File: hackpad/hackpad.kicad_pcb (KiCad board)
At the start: 2 copper layers, 18 parts, among them SW1 SW_Push_45deg, SW2 SW_Push_45deg, SW3 SW_Push_45deg, SW4 SW_Push_45deg, SW5 SW_Push_45deg, SW6 SW_Push_45deg, SW7 SW_Push_45deg, SW8 SW_Push_45deg, SW9 SW_Push_45deg

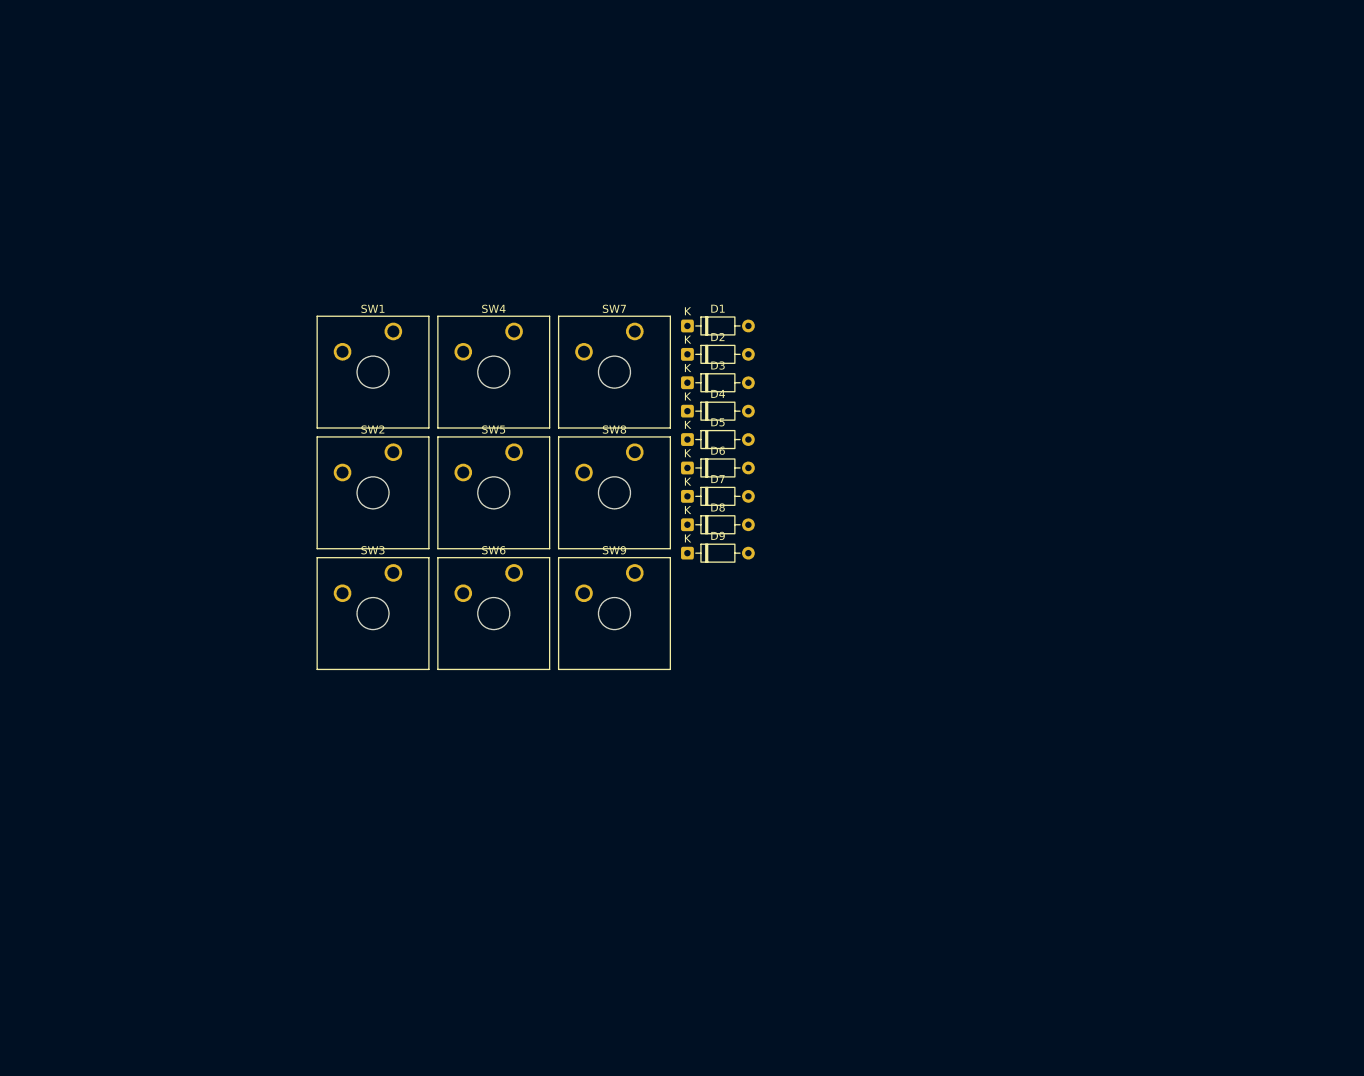
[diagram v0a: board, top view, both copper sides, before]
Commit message: Schematic Complete
Schematic complete currently routing
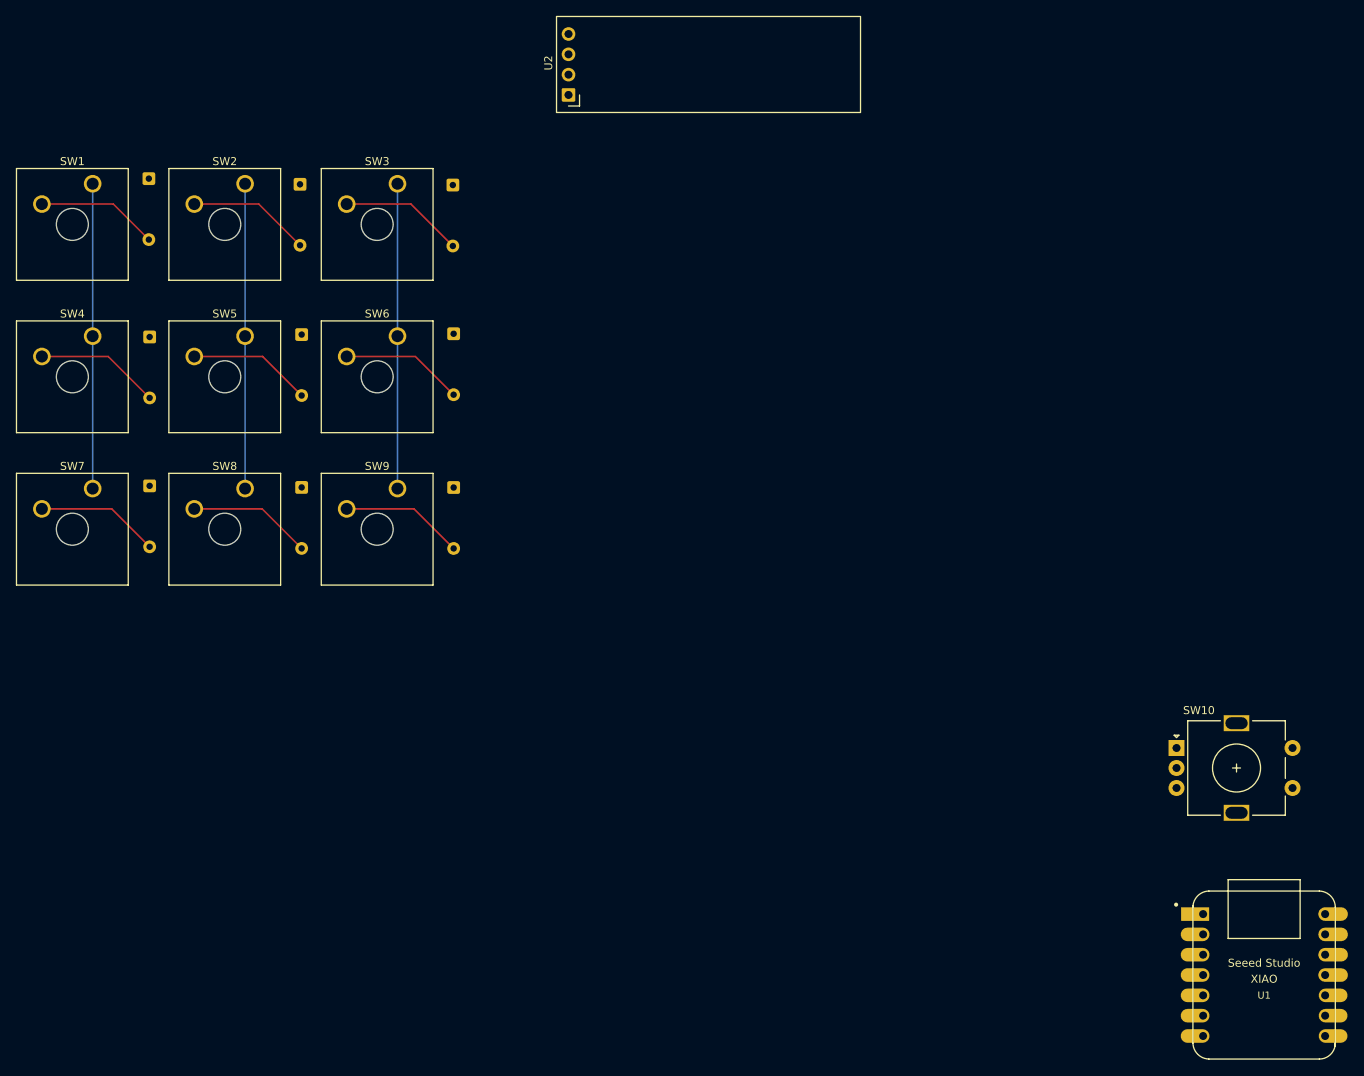
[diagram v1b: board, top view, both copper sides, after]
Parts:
- added SW10: RotaryEncoder_Switch, Rotary_Encoder:RotaryEncoder_Alps_EC11E-Switch_Vertical_H20mm, F.Cu at (185.5, 120.5)
- added U1: MOUDLE-SEEEDUINO-XIAO, footprints:XIAO-Generic-Hybrid-14P-2.54-21X17.8MM, F.Cu at (196.4, 148.9)
- added U2: ER_OLEDM0.91_1x-I2C, Display:ER_OLEDM0.91_1x-I2C, F.Cu at (109.5, 38.9)
- D1, D2, D3, D4, D5, D6, D7, D8, D9: moved to B.Cu
- moved SW7 70.6 mm to (50.0, 88.1)
- moved D1 69.8 mm to (57.0, 49.4), turned to -90 degrees
- moved D4 67.9 mm to (57.1, 69.2), turned to -90 degrees
- moved D7 67.2 mm to (57.1, 87.8), turned to -90 degrees
- moved D2 52.9 mm to (75.9, 50.1), turned to -90 degrees
- moved SW4 52.7 mm to (50.0, 69.0)
- moved D5 50.0 mm to (76.1, 68.8), turned to -90 degrees
- moved SW8 48.9 mm to (69.0, 88.1)
- moved SW3 48.6 mm to (88.1, 50.0)
- moved D8 48.5 mm to (76.1, 88.0), turned to -90 degrees
- moved SW1 41.9 mm to (50.0, 50.0)
- moved D3 38.4 mm to (95.0, 50.2), turned to -90 degrees
- moved SW2 38.3 mm to (69.0, 50.0)
- moved SW5 36.6 mm to (69.0, 69.0)
- moved D6 33.7 mm to (95.1, 68.8), turned to -90 degrees
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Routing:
- net Column 2: track 0.00 -> 38.1 mm
- net Column 1: track 0.00 -> 38.1 mm
- net Column 0: track 0.00 -> 38.1 mm
- net Net-(D4-A): track 0.00 -> 15.6 mm
- net Net-(D8-A): track 0.00 -> 15.5 mm
- net Net-(D5-A): track 0.00 -> 15.4 mm
- net Net-(D3-A): track 0.00 -> 15.4 mm
- net Net-(D7-A): track 0.00 -> 15.4 mm
- net Net-(D9-A): track 0.00 -> 15.4 mm
- net Net-(D2-A): track 0.00 -> 15.4 mm
- net Net-(D6-A): track 0.00 -> 15.3 mm
- net Net-(D1-A): track 0.00 -> 15.2 mm
